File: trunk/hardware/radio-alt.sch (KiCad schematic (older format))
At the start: 19 parts, among them U3 AT86RF231, Y1 NX3225SA-16MHz-15ppm

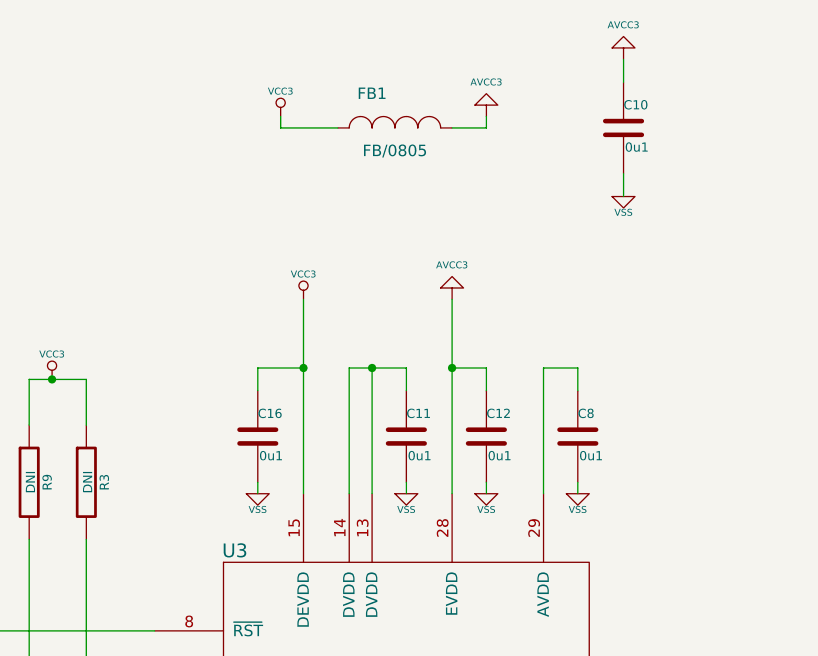
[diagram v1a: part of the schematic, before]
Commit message: Numberous more problems with the circuit design and PCB layout errors found and corrected as a result of debugging and making the RF section work, today, finally.
There remains and issue with the SPI port disable jumper not working as it should -- I think.  I got around this by fluke, when I realised that holding down the reset button (somehow) enables my AVR ISP mkII to program the AVR chip, despite the suspected SPI bus conflict between the ISP and level shofter chip. (Not that any of that makes sense to me right now. But that's what seemed to be the case, at the time. I'll sort it later.)
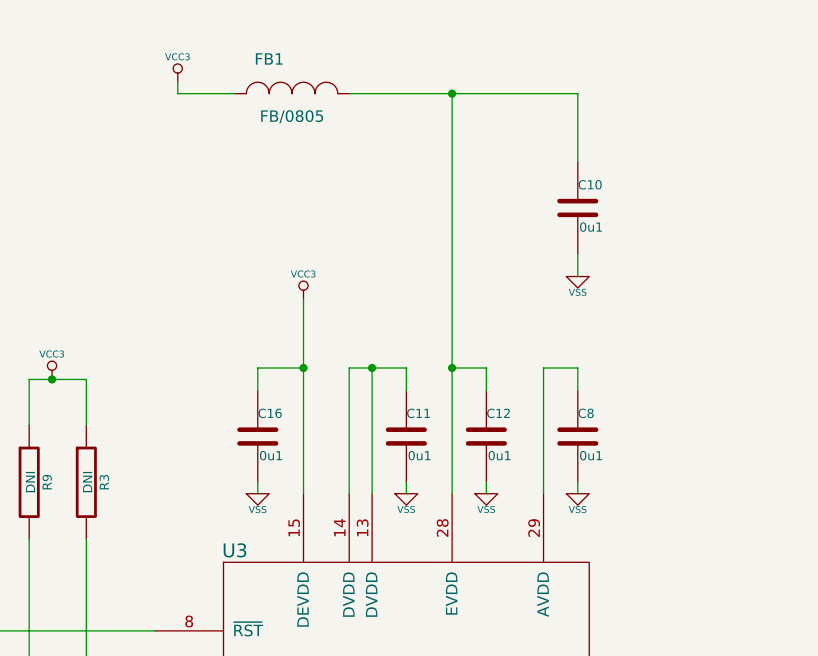
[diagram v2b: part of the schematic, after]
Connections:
- net AVCC: no longer names the net of C10.1, C12.1, FB1.2, U3.28 (EVDD)
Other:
- moved on the sheet: C10, FB1
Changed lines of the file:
@@
 Sheet 2 6
 Title "FREAKDUINO-CHIBI 2.4GHz"
-Date "13 aug 2013"
+Date "16 aug 2013"
 Rev "v1.1"
 Comp "KiCAD version by Gruvin"
@@
 L INDUCTOR_SMALL FB1
 U 1 1 51E3884B
-P 4450 1400
-F 0 "FB1" H 4350 1550 50  0000 C CNN
-F 1 "FB/0805" H 4450 1300 50  0000 C CNN
-F 2 "" H 4450 1400 60  0000 C CNN
-F 3 "" H 4450 1400 60  0000 C CNN
-	1    4450 1400
+P 4000 1250
+F 0 "FB1" H 3900 1400 50  0000 C CNN
+F 1 "FB/0805" H 4000 1150 50  0000 C CNN
+F 2 "" H 4000 1250 60  0000 C CNN
+F 3 "" H 4000 1250 60  0000 C CNN
+	1    4000 1250
 	1    0    0    -1
 $EndComp
@@
 L VCC3 #PWR011
 U 1 1 51E3885A
-P 3950 1350
-F 0 "#PWR011" H 3950 1490 20  0001 C CNN
-F 1 "VCC3" H 3950 1460 30  0000 C CNN
-F 2 "" H 3950 1350 60  0000 C CNN
-F 3 "" H 3950 1350 60  0000 C CNN
-	1    3950 1350
+P 3500 1200
+F 0 "#PWR011" H 3500 1340 20  0001 C CNN
+F 1 "VCC3" H 3500 1310 30  0000 C CNN
+F 2 "" H 3500 1200 60  0000 C CNN
+F 3 "" H 3500 1200 60  0000 C CNN
+	1    3500 1200
 	1    0    0    -1
 $EndComp
@@
 DNI = "DO NOT INSTALL"
 Wire Wire Line
-	4200 1400 3950 1400
-Wire Wire Line
-	3950 1400 3950 1350
-Wire Wire Line
-	4700 2150 4700 3000
+	3750 1250 3500 1250
+Wire Wire Line
+	3500 1250 3500 1200
 Wire Wire Line
 	4250 3000 4250 2450
@@
 	4450 5700 4450 5950
 Wire Wire Line
-	4700 1400 4850 1400
-Wire Wire Line
-	4850 1400 4850 1350
-$Comp
-L AVCC3 #PWR027
-U 1 1 51E8CDB0
-P 4700 2150
-F 0 "#PWR027" H 4700 2350 20  0001 C CNN
-F 1 "AVCC3" H 4700 2300 30  0000 C CNN
-F 2 "~" H 4700 2150 60  0000 C CNN
-F 3 "~" H 4700 2150 60  0000 C CNN
-	1    4700 2150
-	1    0    0    -1
-$EndComp
-$Comp
-L AVCC3 #PWR028
-U 1 1 51E8CDBD
-P 4850 1350
-F 0 "#PWR028" H 4850 1550 20  0001 C CNN
-F 1 "AVCC3" H 4850 1500 30  0000 C CNN
-F 2 "~" H 4850 1350 60  0000 C CNN
-F 3 "~" H 4850 1350 60  0000 C CNN
-	1    4850 1350
-	1    0    0    -1
-$EndComp
-Wire Wire Line
 	4050 2150 4050 3000
 Wire Wire Line
 	1850 4900 3400 4900
-$Comp
-L AVCC3 #PWR030
-U 1 1 51E8CDC3
-P 5450 1100
-F 0 "#PWR030" H 5450 1300 20  0001 C CNN
-F 1 "AVCC3" H 5450 1250 30  0000 C CNN
-F 2 "~" H 5450 1100 60  0000 C CNN
-F 3 "~" H 5450 1100 60  0000 C CNN
-	1    5450 1100
-	1    0    0    -1
-$EndComp
-Wire Wire Line
-	5450 1600 5450 1700
-Wire Wire Line
-	5450 1100 5450 1200
-$Comp
-L VSS #PWR021
+Wire Wire Line
+	5250 1950 5250 2050
+$Comp
+L VSS #PWR027
 U 1 1 51E39C73
-P 5450 1700
-F 0 "#PWR021" H 5450 1700 30  0001 C CNN
-F 1 "VSS" H 5450 1630 30  0000 C CNN
-F 2 "" H 5450 1700 60  0000 C CNN
-F 3 "" H 5450 1700 60  0000 C CNN
-	1    5450 1700
+P 5250 2050
+F 0 "#PWR027" H 5250 2050 30  0001 C CNN
+F 1 "VSS" H 5250 1980 30  0000 C CNN
+F 2 "" H 5250 2050 60  0000 C CNN
+F 3 "" H 5250 2050 60  0000 C CNN
+	1    5250 2050
 	1    0    0    -1
 $EndComp
@@
 L C C10
 U 1 1 51E39C21
-P 5450 1400
-F 0 "C10" H 5450 1500 40  0000 L CNN
-F 1 "0u1" H 5456 1315 40  0000 L CNN
-F 2 "" H 5488 1250 30  0000 C CNN
-F 3 "" H 5450 1400 60  0000 C CNN
-	1    5450 1400
-	1    0    0    -1
-$EndComp
+P 5250 1750
+F 0 "C10" H 5250 1850 40  0000 L CNN
+F 1 "0u1" H 5256 1665 40  0000 L CNN
+F 2 "" H 5288 1600 30  0000 C CNN
+F 3 "" H 5250 1750 60  0000 C CNN
+	1    5250 1750
+	1    0    0    -1
+$EndComp
+Wire Wire Line
+	4700 1250 4700 3000
+Wire Wire Line
+	4250 1250 5250 1250
+Wire Wire Line
+	5250 1250 5250 1550
+Connection ~ 4700 1250
 $EndSCHEMATC

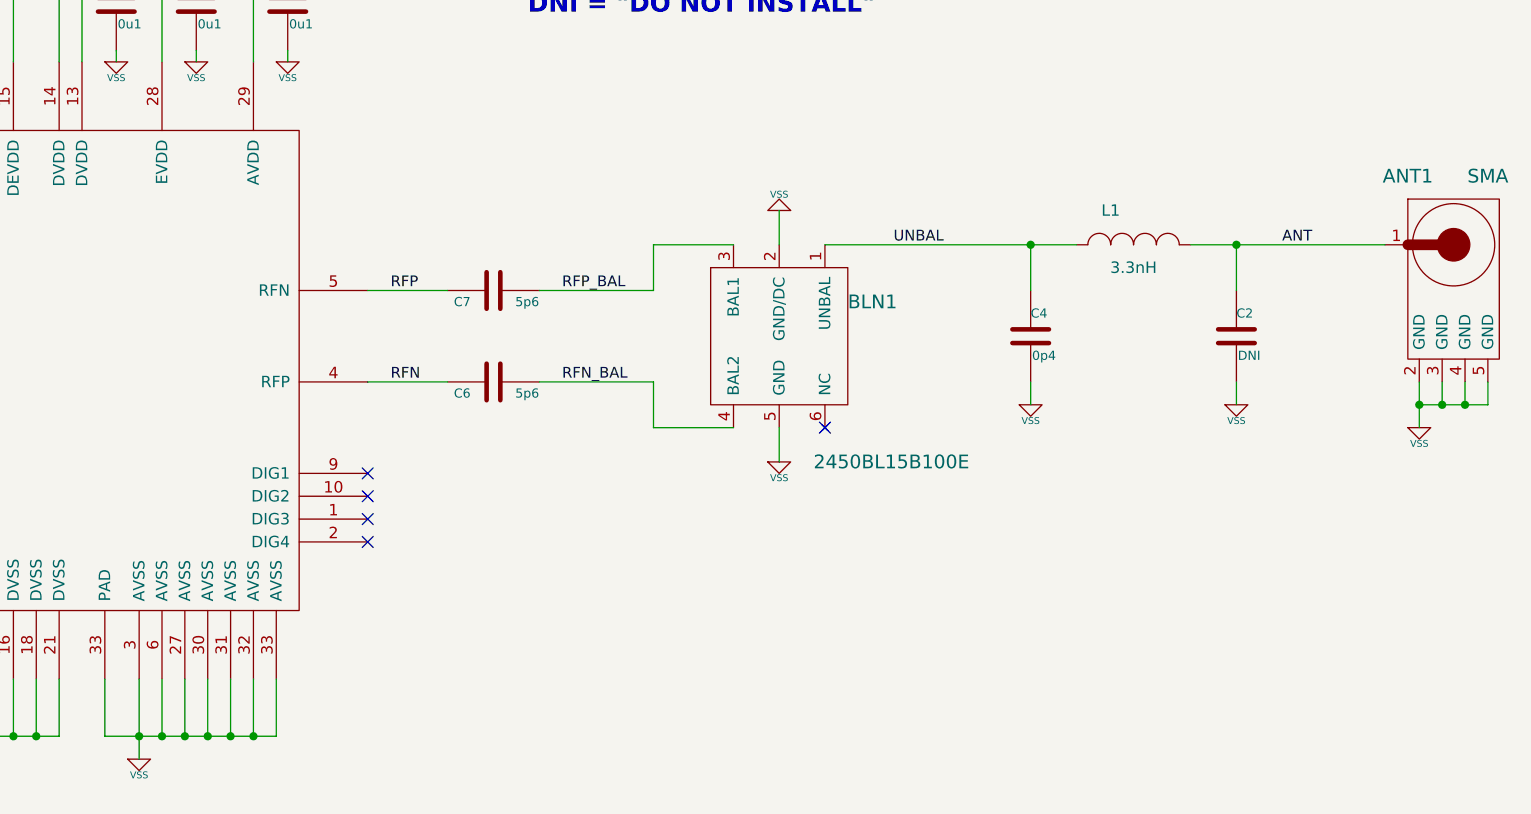
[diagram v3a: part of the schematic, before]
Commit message: Re-worked the RF transmission line circuitry.
I'm frustrated. I've searched high and low for line impedance calculators and I
keep getting the same answers I did the first time around. But my tracks are
much more narrow and more closely spaced than Akiba's -- and my RF section has
massive attenuation. Evidently, his version works well and mine quite simply
does not.  Thus, I've now had no choice but to blindly copy his design, as best
I can and hope for the best. 

This is NOT how I like to do things. I want to understand what I am doing and
why.  So, I will keep trying to find the answers, of course. Meanwhile, I want
this particular project DONE.
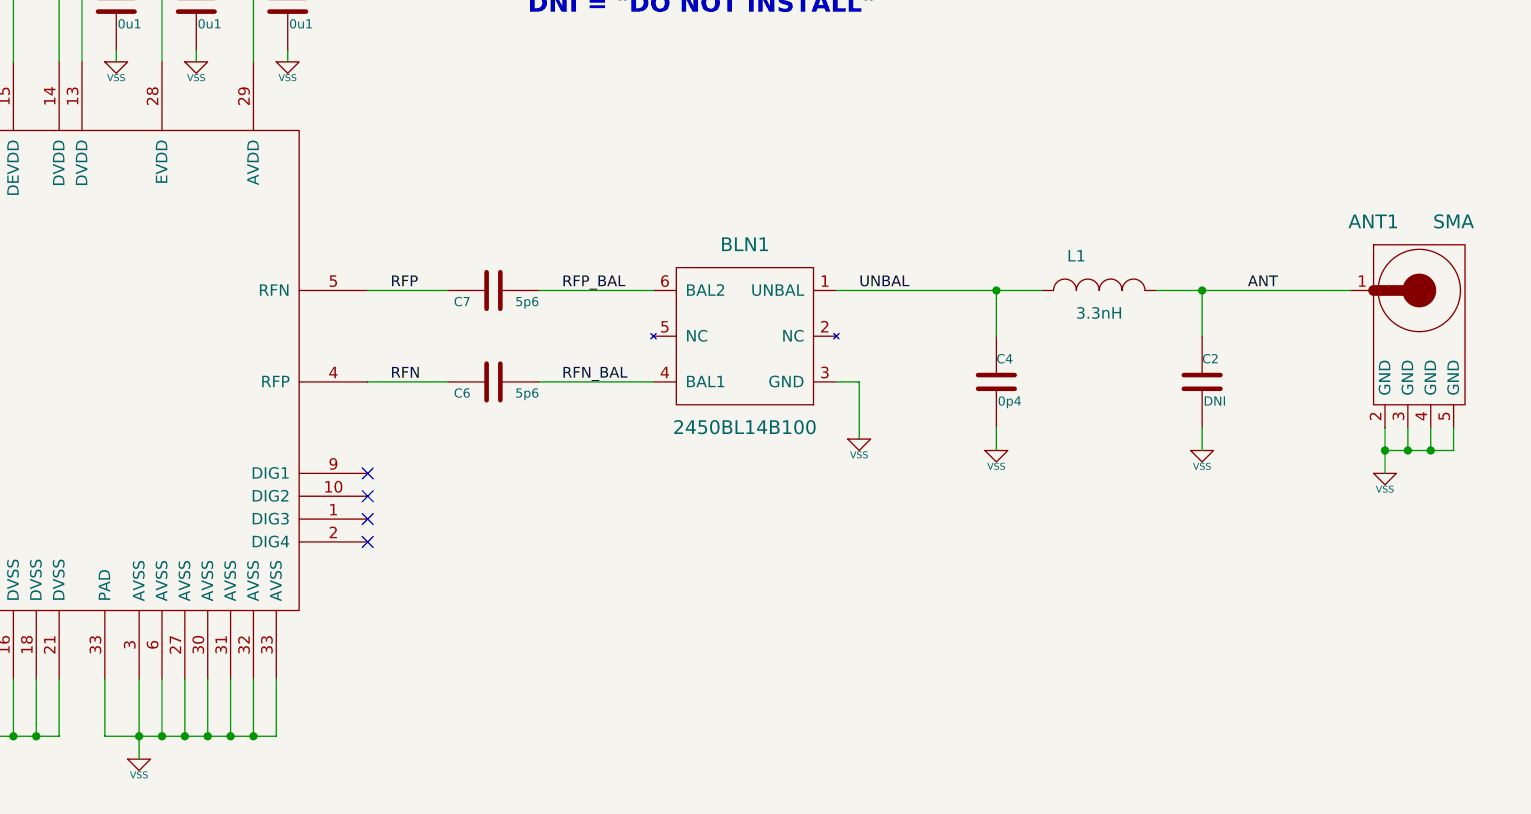
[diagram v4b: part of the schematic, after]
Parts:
- removed BLN1: 2450BL15B100E, ~, symbol BALUN_GRUVIN
- added BLN1: 2450BL14B100, ~, symbol BALUN_2450BL14B100
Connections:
- net RFN_BAL: now also BLN1.4 (BAL1)
- net RFP_BAL: now also BLN1.6 (BAL2)
- net UNBAL: now also BLN1.1 (UNBAL)
- net VSS: now also BLN1.3 (GND)
- no-connect marks 6 -> 5
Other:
- moved on the sheet: ANT1, C2, C4, L1
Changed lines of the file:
@@
 Sheet 2 6
 Title "FREAKDUINO-CHIBI 2.4GHz"
-Date "16 aug 2013"
+Date "17 aug 2013"
 Rev "v1.2"
 Comp "KiCAD version by Gruvin"
@@
 L INDUCTOR_SMALL L1
 U 1 1 51E3A3E1
-P 8950 3800
-F 0 "L1" H 8850 3950 50  0000 C CNN
-F 1 "3.3nH" H 8950 3700 50  0000 C CNN
-F 2 "" H 8950 3800 60  0000 C CNN
-F 3 "" H 8950 3800 60  0000 C CNN
-	1    8950 3800
+P 8800 4000
+F 0 "L1" H 8700 4150 50  0000 C CNN
+F 1 "3.3nH" H 8800 3900 50  0000 C CNN
+F 2 "" H 8800 4000 60  0000 C CNN
+F 3 "" H 8800 4000 60  0000 C CNN
+	1    8800 4000
 	1    0    0    -1
 $EndComp
@@
 L C C4
 U 1 1 51E3A3F1
-P 8500 4200
-F 0 "C4" H 8500 4300 40  0000 L CNN
-F 1 "0p4" H 8506 4115 40  0000 L CNN
-F 2 "" H 8538 4050 30  0000 C CNN
-F 3 "" H 8500 4200 60  0000 C CNN
-	1    8500 4200
+P 8350 4400
+F 0 "C4" H 8350 4500 40  0000 L CNN
+F 1 "0p4" H 8356 4315 40  0000 L CNN
+F 2 "" H 8388 4250 30  0000 C CNN
+F 3 "" H 8350 4400 60  0000 C CNN
+	1    8350 4400
 	1    0    0    -1
 $EndComp
@@
 L C C2
 U 1 1 51E3A3F7
-P 9400 4200
-F 0 "C2" H 9400 4300 40  0000 L CNN
-F 1 "DNI" H 9406 4115 40  0000 L CNN
-F 2 "" H 9438 4050 30  0000 C CNN
-F 3 "" H 9400 4200 60  0000 C CNN
-	1    9400 4200
-	1    0    0    -1
-$EndComp
-Text Label 7900 3800 0    47   ~ 0
+P 9250 4400
+F 0 "C2" H 9250 4500 40  0000 L CNN
+F 1 "DNI" H 9256 4315 40  0000 L CNN
+F 2 "" H 9288 4250 30  0000 C CNN
+F 3 "" H 9250 4400 60  0000 C CNN
+	1    9250 4400
+	1    0    0    -1
+$EndComp
+Text Label 7750 4000 0    47   ~ 0
 UNBAL
-Text Label 9600 3800 0    47   ~ 0
+Text Label 9450 4000 0    47   ~ 0
 ANT
 $Comp
 L VSS #PWR021
 U 1 1 51E3A542
-P 8500 4500
-F 0 "#PWR021" H 8500 4500 30  0001 C CNN
-F 1 "VSS" H 8500 4430 30  0000 C CNN
-F 2 "" H 8500 4500 60  0000 C CNN
-F 3 "" H 8500 4500 60  0000 C CNN
-	1    8500 4500
+P 8350 4700
+F 0 "#PWR021" H 8350 4700 30  0001 C CNN
+F 1 "VSS" H 8350 4630 30  0000 C CNN
+F 2 "" H 8350 4700 60  0000 C CNN
+F 3 "" H 8350 4700 60  0000 C CNN
+	1    8350 4700
 	1    0    0    -1
 $EndComp
@@
 L VSS #PWR022
 U 1 1 51E3A548
-P 9400 4500
-F 0 "#PWR022" H 9400 4500 30  0001 C CNN
-F 1 "VSS" H 9400 4430 30  0000 C CNN
-F 2 "" H 9400 4500 60  0000 C CNN
-F 3 "" H 9400 4500 60  0000 C CNN
-	1    9400 4500
+P 9250 4700
+F 0 "#PWR022" H 9250 4700 30  0001 C CNN
+F 1 "VSS" H 9250 4630 30  0000 C CNN
+F 2 "" H 9250 4700 60  0000 C CNN
+F 3 "" H 9250 4700 60  0000 C CNN
+	1    9250 4700
 	1    0    0    -1
 $EndComp
@@
 L VSS #PWR023
 U 1 1 51E3A80A
-P 7400 4750
-F 0 "#PWR023" H 7400 4750 30  0001 C CNN
-F 1 "VSS" H 7400 4680 30  0000 C CNN
-F 2 "" H 7400 4750 60  0000 C CNN
-F 3 "" H 7400 4750 60  0000 C CNN
-	1    7400 4750
+P 7750 4650
+F 0 "#PWR023" H 7750 4650 30  0001 C CNN
+F 1 "VSS" H 7750 4580 30  0000 C CNN
+F 2 "" H 7750 4650 60  0000 C CNN
+F 3 "" H 7750 4650 60  0000 C CNN
+	1    7750 4650
 	1    0    0    -1
 $EndComp
@@
 L SMA ANT1
 U 1 1 51E3A9AC
-P 10350 4050
-F 0 "ANT1" H 10150 4600 60  0000 C CNN
-F 1 "SMA" H 10500 4600 60  0000 C CNN
-F 2 "" H 10350 4050 60  0000 C CNN
-F 3 "" H 10350 4050 60  0000 C CNN
-	1    10350 4050
+P 10200 4250
+F 0 "ANT1" H 10000 4800 60  0000 C CNN
+F 1 "SMA" H 10350 4800 60  0000 C CNN
+F 2 "" H 10200 4250 60  0000 C CNN
+F 3 "" H 10200 4250 60  0000 C CNN
+	1    10200 4250
 	1    0    0    -1
 $EndComp
@@
 L VSS #PWR024
 U 1 1 51E3A9B9
-P 10200 4600
-F 0 "#PWR024" H 10200 4600 30  0001 C CNN
-F 1 "VSS" H 10200 4530 30  0000 C CNN
-F 2 "" H 10200 4600 60  0000 C CNN
-F 3 "" H 10200 4600 60  0000 C CNN
-	1    10200 4600
+P 10050 4800
+F 0 "#PWR024" H 10050 4800 30  0001 C CNN
+F 1 "VSS" H 10050 4730 30  0000 C CNN
+F 2 "" H 10050 4800 60  0000 C CNN
+F 3 "" H 10050 4800 60  0000 C CNN
+	1    10050 4800
 	1    0    0    -1
 $EndComp
@@
 	1    0    0    -1
 $EndComp
-$Comp
-L BALUN_GRUVIN BLN1
-U 1 1 51E793F4
-P 7400 4200
-F 0 "BLN1" H 7700 4350 60  0000 L CNN
-F 1 "2450BL15B100E" H 7550 3650 60  0000 L CNN
-F 2 "~" H 7400 4200 60  0000 C CNN
-F 3 "~" H 7400 4200 60  0000 C CNN
-	1    7400 4200
-	1    0    0    -1
-$EndComp
-$Comp
-L VSS #PWR026
-U 1 1 51E79531
-P 7400 3650
-F 0 "#PWR026" H 7400 3650 30  0001 C CNN
-F 1 "VSS" H 7400 3580 30  0000 C CNN
-F 2 "" H 7400 3650 60  0000 C CNN
-F 3 "" H 7400 3650 60  0000 C CNN
-	1    7400 3650
-	-1   0    0    1
-$EndComp
-NoConn ~ 7600 4600
 Text Notes 6300 2800 0    79   ~ 16
 DNI = "DO NOT INSTALL"
@@
 	4600 5700 4600 6050
 Wire Wire Line
-	4700 5700 4700 5950
+	4700 5950 4700 5700
 Wire Wire Line
 	4450 5950 5200 5950
@@
 	6850 4400 6350 4400
 Wire Wire Line
-	7600 3800 8700 3800
-Wire Wire Line
-	8500 4000 8500 3800
-Connection ~ 8500 3800
-Wire Wire Line
-	9200 3800 10050 3800
-Wire Wire Line
-	9400 4000 9400 3800
-Connection ~ 9400 3800
-Wire Wire Line
-	8500 4500 8500 4400
-Wire Wire Line
-	9400 4400 9400 4500
-Wire Wire Line
-	7400 4600 7400 4750
-Wire Wire Line
-	10200 4400 10200 4600
-Wire Wire Line
-	10300 4400 10300 4500
-Wire Wire Line
-	10200 4500 10500 4500
-Connection ~ 10200 4500
-Wire Wire Line
-	10400 4500 10400 4400
-Connection ~ 10300 4500
-Wire Wire Line
-	10500 4500 10500 4400
-Connection ~ 10400 4500
+	7650 4000 8550 4000
+Wire Wire Line
+	8350 4200 8350 4000
+Connection ~ 8350 4000
+Wire Wire Line
+	9050 4000 9900 4000
+Wire Wire Line
+	9250 4200 9250 4000
+Connection ~ 9250 4000
+Wire Wire Line
+	8350 4700 8350 4600
+Wire Wire Line
+	9250 4600 9250 4700
+Wire Wire Line
+	10050 4600 10050 4800
+Wire Wire Line
+	10150 4600 10150 4700
+Wire Wire Line
+	10050 4700 10350 4700
+Connection ~ 10050 4700
+Wire Wire Line
+	10250 4700 10250 4600
+Connection ~ 10150 4700
+Wire Wire Line
+	10350 4700 10350 4600
+Connection ~ 10250 4700
 Wire Wire Line
 	3850 2550 3850 2450
@@
 	3850 3000 3850 2950
 Wire Wire Line
-	6850 4000 6850 3800
-Wire Wire Line
-	6850 3800 7200 3800
-Wire Wire Line
-	6850 4400 6850 4600
-Wire Wire Line
-	6850 4600 7200 4600
-Wire Wire Line
-	7400 3800 7400 3650
-Wire Wire Line
 	4450 5700 4450 5950
 Wire Wire Line
@@
 	5250 1950 5250 2050
 $Comp
-L VSS #PWR027
+L VSS #PWR026
 U 1 1 51E39C73
 P 5250 2050
-F 0 "#PWR027" H 5250 2050 30  0001 C CNN
+F 0 "#PWR026" H 5250 2050 30  0001 C CNN
 F 1 "VSS" H 5250 1980 30  0000 C CNN
 F 2 "" H 5250 2050 60  0000 C CNN
@@
 	5250 1250 5250 1550
 Connection ~ 4700 1250
+$Comp
+L BALUN_2450BL14B100 BLN1
+U 1 1 520EF4AD
+P 7250 4400
+F 0 "BLN1" H 7250 5000 60  0000 C CNN
+F 1 "2450BL14B100" H 7250 4200 60  0000 C CNN
+F 2 "~" V 7250 4600 60  0000 C CNN
+F 3 "~" V 7250 4600 60  0000 C CNN
+	1    7250 4400
+	1    0    0    -1
+$EndComp
+Wire Wire Line
+	7750 4650 7750 4400
+Wire Wire Line
+	7750 4400 7650 4400
 $EndSCHEMATC
